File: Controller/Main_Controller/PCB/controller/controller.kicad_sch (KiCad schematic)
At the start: 252 parts, among them J1 Conn_01x10, M1 Motor_DC, Q1 S9013, Q10 S9013, Q11 S9013, Q12 S9013, Q13 S9013, Q14 S9013, Q15 S9013, Q16 S9013, Q17 S9013, Q18 S9013, Q19 S9013, Q2 S9013, Q20 S9013, Q21 S9013, Q22 S9013, Q23 S9013, Q24 S9013, Q25 Q_PMOS_DGS, Q26 Q_NMOS_DGS, Q27 S9013, Q3 S9013, Q4 S9013, Q5 S9013, Q6 S9013, Q7 S9013, Q8 S9013, Q9 S9013, SW1 SW_SPDT, SW2 SW_SPDT, U1 NUCLEO-L432KC, U10 ZLDO1117G50TA, U2 NUCLEO144-F429ZI, U3 74HC14, U4 74HC14, U5 74HC14, U6 Joystick, U7 Joystick, U8 HY1602E, U9 ZSR330GTA

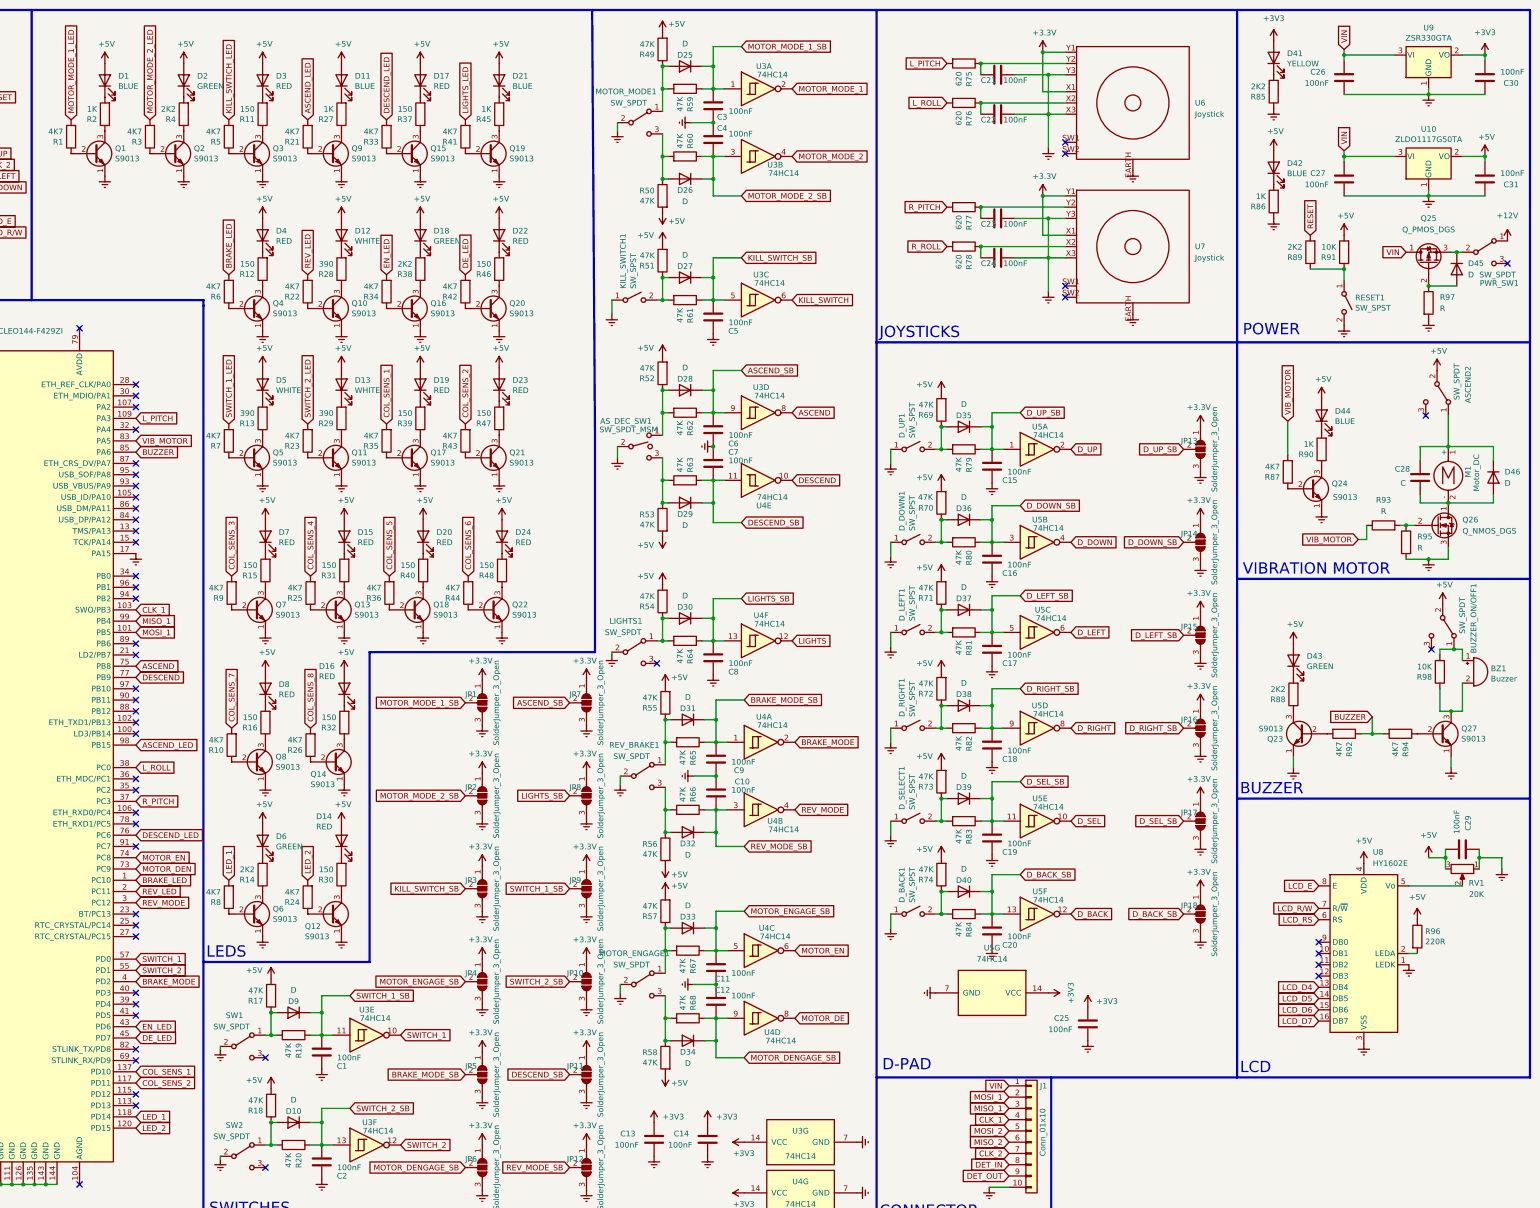
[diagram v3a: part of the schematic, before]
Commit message: Finished footprints on the schematic.
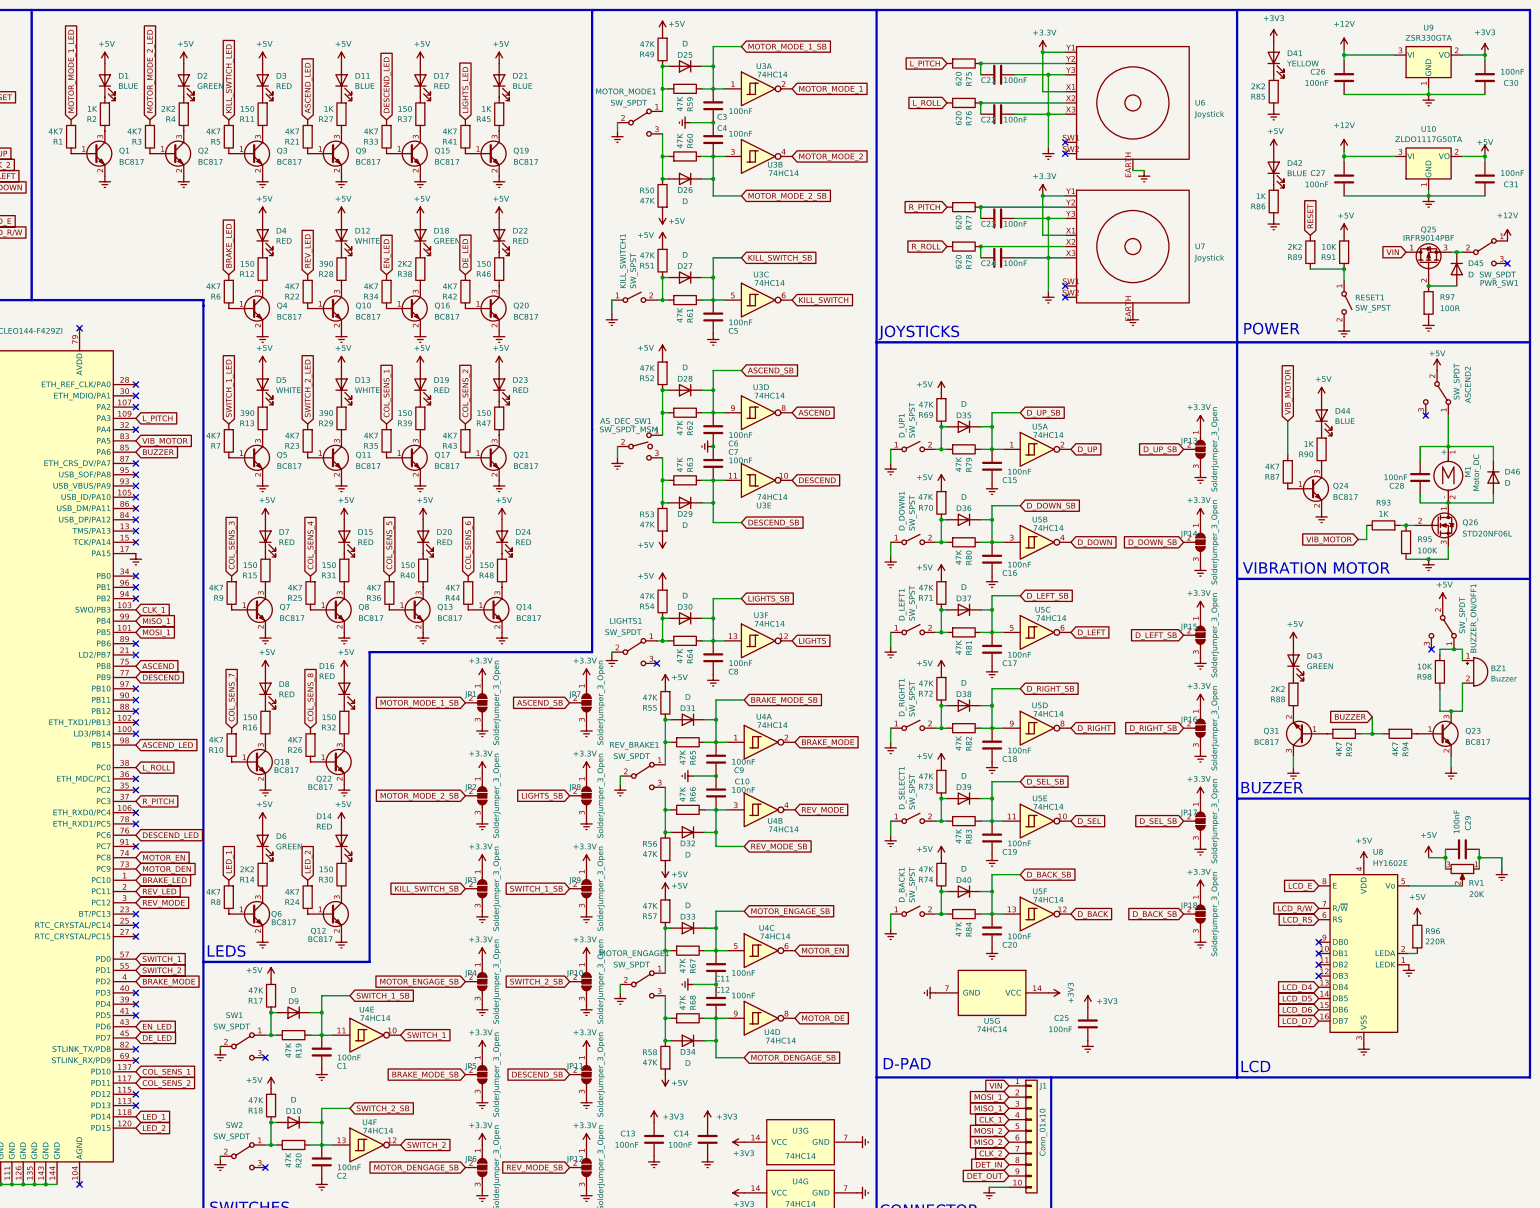
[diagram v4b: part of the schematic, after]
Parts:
- removed Q1, Q10, Q11, Q12, Q13, Q14, Q15, Q16, Q17, Q18, Q19, Q2, Q20, Q21, Q22, Q23, Q24, Q27, Q3, Q4, Q5, Q6, Q7, Q8, Q9: S9013, Package_TO_SOT_SMD:SOT-23, symbol Transistor_BJT:2N2219
- added Q1, Q10, Q11, Q12, Q13, Q14, Q15, Q16, Q17, Q18, Q19, Q2, Q20, Q21, Q22, Q23, Q24, Q3, Q31, Q4, Q5, Q6, Q7, Q8, Q9: BC817, Package_TO_SOT_SMD:SOT-23, symbol Transistor_BJT:BC817
- ASCEND2, AS_DEC_SW1, BUZZER_ON/OFF1, LIGHTS1, MOTOR_ENGAGE1, MOTOR_MODE1, REV_BRAKE1, SW1, SW2: footprint (none) -> My_library:1Ms1T1B1M1QE
- C28: value C -> 100nF; footprint (none) -> Capacitor_SMD:C_0603_1608Metric
- D10, D25, D26, D27, D28, D29, D30, D31, D32, D33, D34, D35, D36, D37, D38, D39, D40, D45, D46, D9: footprint (none) -> Diode_SMD:D_SMA
- J1: footprint (none) -> Connector_PinHeader_1.27mm:PinHeader_1x10_P1.27mm_Vertical
- JP1, JP10, JP11, JP12, JP13, JP14, JP15, JP16, JP17, JP18, JP2, JP3, JP4, JP5, JP6, JP7, JP8, JP9: footprint (none) -> Jumper:SolderJumper-3_P1.3mm_Open_RoundedPad1.0x1.5mm_NumberLabels
- M1: footprint (none) -> Motors:Vybronics_VZ30C1T8219732L
- Q25: value Q_PMOS_DGS -> IRFR9014PBF; footprint (none) -> My_library:STD20NF06L
- Q26: value Q_NMOS_DGS -> STD20NF06L; footprint (none) -> My_library:STD20NF06L
- R93: value R -> 1K; footprint (none) -> Resistor_SMD:R_0201_0603Metric
- R95: value R -> 100K; footprint (none) -> Resistor_SMD:R_0201_0603Metric
- R97: value R -> 100R; footprint (none) -> Resistor_SMD:R_0201_0603Metric
- U1: footprint (none) -> Module:Arduino_Nano
- U3: renamed from U4; footprint (none) -> Package_SO:SO-14_3.9x8.65mm_P1.27mm
- U3, U4, U5: footprint (none) -> Package_SO:SO-14_3.9x8.65mm_P1.27mm
- U4: renamed from U3; footprint (none) -> Package_SO:SO-14_3.9x8.65mm_P1.27mm
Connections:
- net +12V: now also C26.1, C27.1, U10.3 (VI), U9.3 (VI)
- net Earth: now also Q1.2 (E), Q10.2 (E), Q11.2 (E), Q12.2 (E), Q13.2 (E), Q14.2 (E), Q15.2 (E), Q16.2 (E), Q17.2 (E), Q18.2 (E), Q19.2 (E), Q2.2 (E), Q20.2 (E), Q21.2 (E), Q22.2 (E), Q23.2 (E), Q24.2 (E), Q3.2 (E), Q31.3 (C), Q4.2 (E), Q5.2 (E), Q6.2 (E), Q7.2 (E), Q8.2 (E), Q9.2 (E)
- net VIN: no longer C26.1, C27.1, U10.3 (VI), U9.3 (VI)
- net at R1.1: now also Q1.1 (B)
- net at R2.1: now also Q1.3 (C)
- net at R8.1: now also Q6.1 (B)
- net at R14.1: now also Q6.3 (C)
- net at R10.1: now also Q18.1 (B)
- net at R16.1: now also Q18.3 (C)
- net at R26.1: now also Q22.1 (B)
- net at R33.1: now also Q15.1 (B)
- net at R6.1: now also Q4.1 (B)
- net at R29.1: now also Q11.3 (C)
- net at R5.1: now also Q3.1 (B)
- net at R11.1: now also Q3.3 (C)
- net at R48.1: now also Q14.3 (C)
- net at R94.1: now also Q23.1 (B)
- net at BZ1.2 (+), R98.1: now also Q23.3 (C)
- net at R9.1: now also Q7.1 (B)
- net at R15.1: now also Q7.3 (C)
- net at R21.1: now also Q9.1 (B)
- net at R34.1: now also Q16.1 (B)
- net at R38.1: now also Q16.3 (C)
- net at R35.1: now also Q17.1 (B)
- net at R25.1: now also Q8.1 (B)
- net at R31.1: now also Q8.3 (C)
- net at R41.1: now also Q19.1 (B)
- net at R45.1: now also Q19.3 (C)
- net at R4.1: now also Q2.3 (C)
- net at R32.1: now also Q22.3 (C)
- net at ASCEND2.1 (A), D46.1 (K), M1.1 (+): now also C28.2; no longer C28.1
- net at D46.2 (A), M1.2 (-), Q26.1 (D): now also C28.1; no longer C28.2
- net at R40.1: now also Q13.3 (C)
- net at R43.1: now also Q21.1 (B)
- net at R47.1: now also Q21.3 (C)
- net at R12.1: now also Q4.3 (C)
- net at R3.1: now also Q2.1 (B)
- net at R39.1: now also Q17.3 (C)
- net at R23.1: now also Q11.1 (B)
- net at R44.1: now also Q14.1 (B)
- net at R7.1: now also Q5.1 (B)
- net at R13.1: now also Q5.3 (C)
- net at R37.1: now also Q15.3 (C)
- net at R22.1: now also Q10.1 (B)
- net at R24.1: now also Q12.1 (B)
- net at R27.1: now also Q9.3 (C)
- net at R30.1: now also Q12.3 (C)
- net at R42.1: now also Q20.1 (B)
- net at R46.1: now also Q20.3 (C)
- net at R88.1: now also Q31.2 (E)
- net at R92.2: now also Q31.1 (B)
- net at R36.1: now also Q13.1 (B)
- net at R87.1: now also Q24.1 (B)
- net at R90.1: now also Q24.3 (C)
- net at R28.1: now also Q10.3 (C)
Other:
- moved on the sheet: C28
